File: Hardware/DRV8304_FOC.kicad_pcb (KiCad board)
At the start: 4 copper layers, 51.5 x 42.8 mm, 64 parts, among them J1 Conn_01x02, J2 Conn_01x03, J3 Conn_01x03, J4 Conn_02x07_Counter_Clockwise, Q1 SIRA18ADP, Q2 SIRA18ADP, Q3 SIRA18ADP, Q4 SIRA18ADP, Q5 SIRA18ADP, Q6 SIRA18ADP, SW2 SW_Push, U1 TPS565208, U2 TPS259850RQPR, U3 DRV8304HRHAR, U4 STM32F412CEUx, U5 AS5055A, Y1 Crystal_GND23

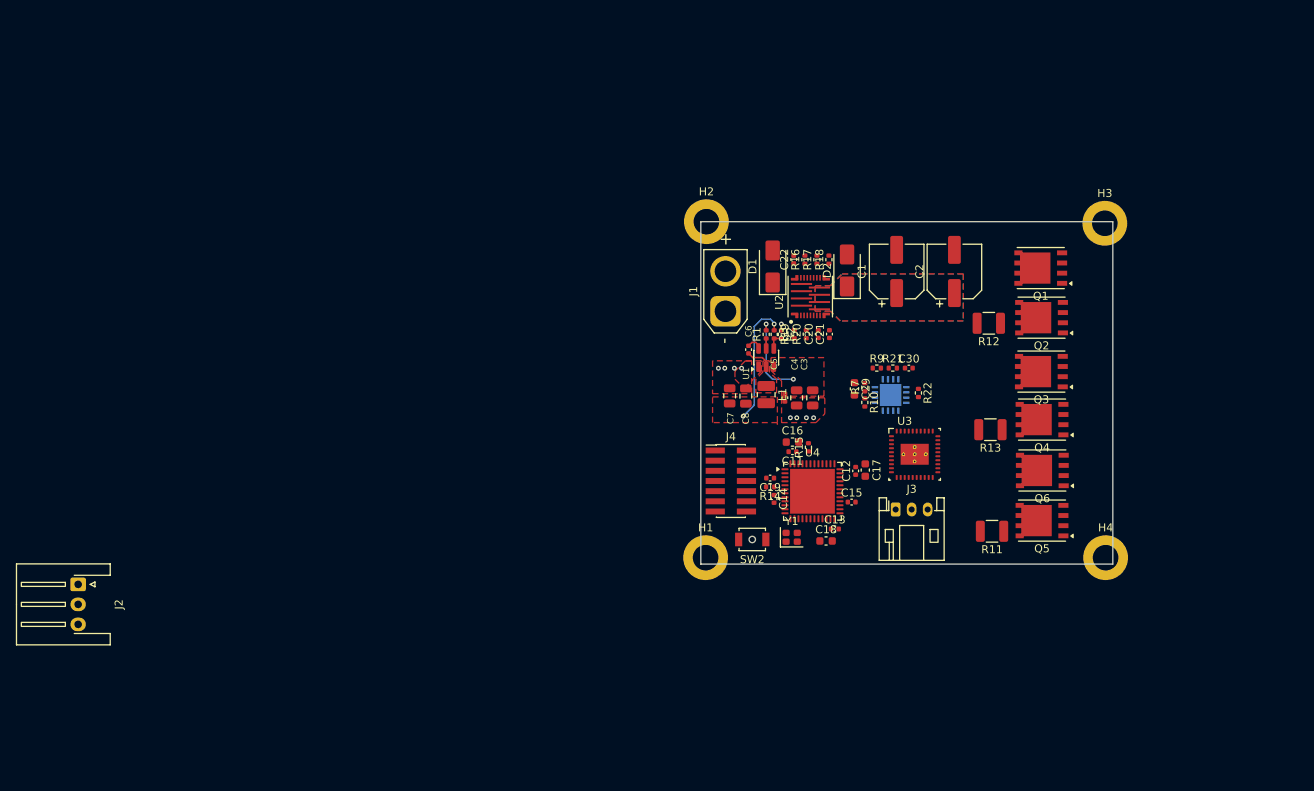
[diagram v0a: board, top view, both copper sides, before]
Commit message: Added Board outline DXF and test points
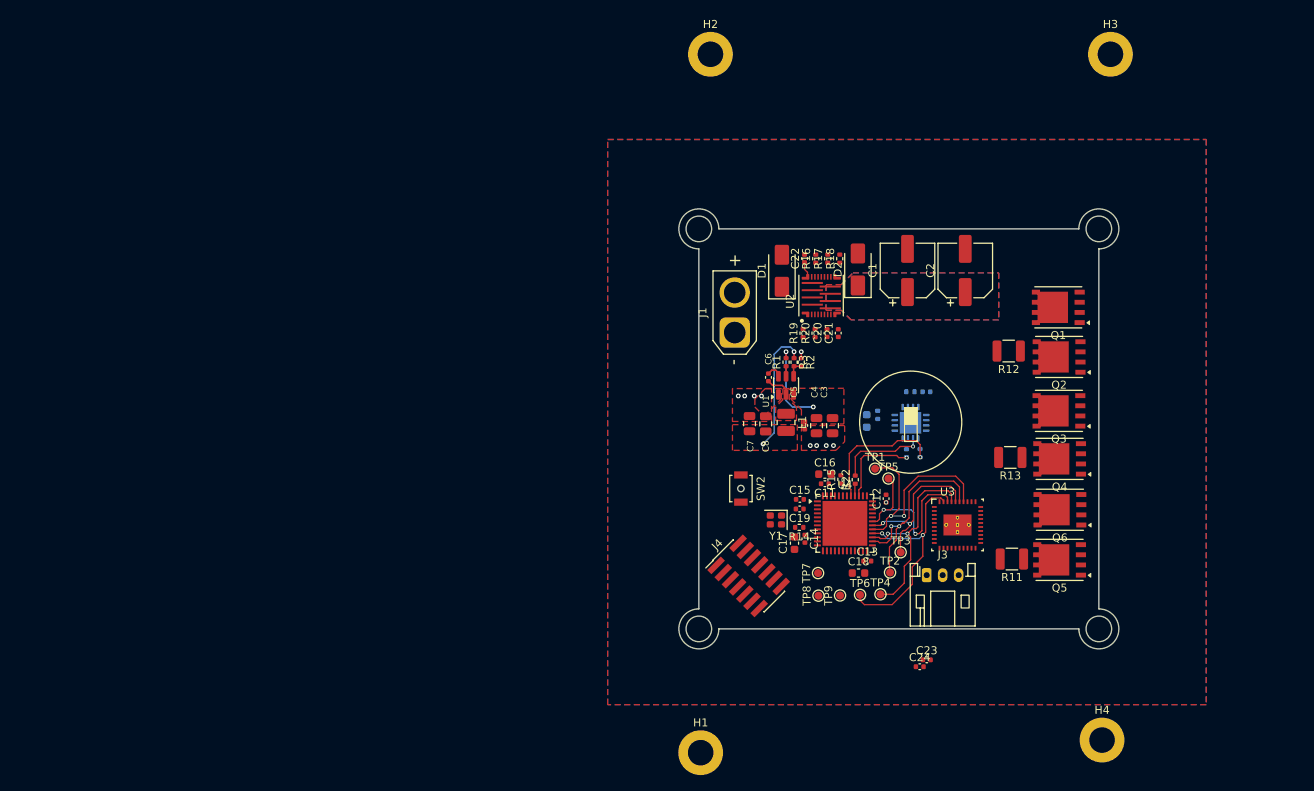
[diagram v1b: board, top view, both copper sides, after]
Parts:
- removed J2: Conn_01x03, Connector_JST:JST_XH_S3B-XH-A-1_1x03_P2.50mm_Horizontal
- added C23: 0.1uF, Capacitor_SMD:C_0402_1005Metric, F.Cu at (164.1, 126.4)
- added C24: 0.1uF, Capacitor_SMD:C_0402_1005Metric, F.Cu at (163.2, 127.3)
- added TP1: TestPoint, TestPoint:TestPoint_Pad_D1.0mm, F.Cu at (157.6, 102.5)
- added TP2: TestPoint, TestPoint:TestPoint_Pad_D1.0mm, F.Cu at (159.5, 115.5)
- added TP3: TestPoint, TestPoint:TestPoint_Pad_D1.0mm, F.Cu at (160.8, 113.0)
- added TP4: TestPoint, TestPoint:TestPoint_Pad_D1.0mm, F.Cu at (158.3, 118.2)
- added TP5: TestPoint, TestPoint:TestPoint_Pad_D1.0mm, F.Cu at (159.3, 103.8)
- added TP6: TestPoint, TestPoint:TestPoint_Pad_D1.0mm, F.Cu at (155.7, 118.3)
- added TP7: TestPoint, TestPoint:TestPoint_Pad_D1.0mm, F.Cu at (150.5, 115.6)
- added TP8: TestPoint, TestPoint:TestPoint_Pad_D1.0mm, F.Cu at (150.5, 118.4)
- added TP9: TestPoint, TestPoint:TestPoint_Pad_D1.0mm, F.Cu at (153.2, 118.4)
- C29, C30, R10, R21, R7, R9: moved to B.Cu
- moved H1 24.4 mm to (135.8, 138.0)
- moved H4 22.8 mm to (186.0, 136.5)
- moved H3 21.1 mm to (187.0, 50.7)
- moved H2 20.9 mm to (137.0, 50.7)
- moved R22 13.4 mm to (155.1, 103.9), turned to 90 degrees
- moved C17 12.7 mm to (147.5, 111.8), turned to 90 degrees
- moved J4 12.1 mm to (141.8, 115.9), turned to 45 degrees
- moved R9 11.9 mm to (163.2, 100.6), turned to 90 degrees
- moved U3 10.3 mm to (167.9, 109.6)
- moved J3 9.08 mm to (164.1, 115.8)
- moved R10 8.21 mm to (161.5, 100.6), turned to 90 degrees
- moved SW2 6.52 mm to (140.8, 105.0), turned to -90 degrees
- moved C15 6.48 mm to (148.2, 106.4)
- moved C14 6.30 mm to (148.8, 111.3)
- moved R14 6.23 mm to (148.1, 109.9)
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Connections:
- J3 pad 1: unconnected-(J3-Pin_1-Pad1) -> GND
- J3 pad 2: unconnected-(J3-Pin_2-Pad2) -> UART_RX
- J3 pad 3: unconnected-(J3-Pin_3-Pad3) -> UART_TX
- Q1 pad 1: Vin -> Net-(Q1-D)
- Q1 pad 2: unconnected-(Q1-G-Pad2) -> Net-(Q1-D)
- Q1 pad 3: Net-(Q1-S) -> Net-(Q1-D)
- Q1 pad 4: (no net) -> GHA
- Q1 pad 5: (no net) -> Vin
- Q2 pad 1: Net-(Q1-S) -> Net-(Q2-D)
- Q2 pad 2: unconnected-(Q2-G-Pad2) -> Net-(Q2-D)
- Q2 pad 3: Net-(Q2-S) -> Net-(Q2-D)
- Q2 pad 4: (no net) -> GLA
- Q2 pad 5: (no net) -> Net-(Q1-D)
- Q3 pad 1: Vin -> Net-(Q3-D)
- Q3 pad 2: unconnected-(Q3-G-Pad2) -> Net-(Q3-D)
- Q3 pad 3: Net-(Q3-S) -> Net-(Q3-D)
- Q3 pad 4: (no net) -> unconnected-(Q3-G-Pad4)
- Q3 pad 5: (no net) -> Vin
- Q4 pad 1: Net-(Q3-S) -> Net-(Q4-D)
- Q4 pad 2: unconnected-(Q4-G-Pad2) -> Net-(Q4-D)
- Q4 pad 3: Net-(Q4-S) -> Net-(Q4-D)
- Q4 pad 4: (no net) -> unconnected-(Q4-G-Pad4)
- Q4 pad 5: (no net) -> Net-(Q3-D)
- Q5 pad 1: Vin -> Net-(Q5-D)
- Q5 pad 2: unconnected-(Q5-G-Pad2) -> Net-(Q5-D)
- Q5 pad 3: Net-(Q5-S) -> Net-(Q5-D)
- Q5 pad 4: (no net) -> unconnected-(Q5-G-Pad4)
- Q5 pad 5: (no net) -> Vin
- Q6 pad 1: Net-(Q5-S) -> Net-(Q6-D)
- Q6 pad 2: unconnected-(Q6-G-Pad2) -> Net-(Q6-D)
- Q6 pad 3: Net-(Q6-S) -> Net-(Q6-D)
- Q6 pad 4: (no net) -> unconnected-(Q6-G-Pad4)
- Q6 pad 5: (no net) -> Net-(Q5-D)
- R10 pad 1: SCK -> SPI_SCK
- R11 pad 1: Net-(Q2-S) -> Net-(Q2-D)
- R12 pad 1: Net-(Q4-S) -> Net-(Q4-D)
- R13 pad 1: Net-(Q6-S) -> Net-(Q6-D)
- R22 pad 1: Net-(U5-MISO) -> Net-(U4-PB4)
- R22 pad 2: MISO -> SPI_MISO
- R9 pad 1: MOSI -> SPI_MOSI
- U3 pad 21: unconnected-(U3-SOC-Pad21) -> ISENSE_C
- U3 pad 22: unconnected-(U3-SOB-Pad22) -> ISENSE_B
- U3 pad 23: unconnected-(U3-SOA-Pad23) -> ISENSE_A
- U3 pad 34: unconnected-(U3-INHA-Pad34) -> INHA
- U3 pad 35: unconnected-(U3-INLA-Pad35) -> INLA
- U3 pad 36: unconnected-(U3-INHB-Pad36) -> INHB
- U3 pad 37: unconnected-(U3-INLB-Pad37) -> INLB
- U3 pad 38: unconnected-(U3-INHC-Pad38) -> INHC
- U3 pad 39: unconnected-(U3-INLC-Pad39) -> INLC
- U4 pad 13: unconnected-(U4-PA3-Pad13) -> ISENSE_C
- U4 pad 14: unconnected-(U4-PA4-Pad14) -> ISENSE_B
- U4 pad 15: unconnected-(U4-PA5-Pad15) -> ISENSE_A
- U4 pad 20: unconnected-(U4-PB2-Pad20) -> SPI_~{SS}
- U4 pad 26: unconnected-(U4-PB13-Pad26) -> INLA
- U4 pad 27: unconnected-(U4-PB14-Pad27) -> INLB
- U4 pad 28: unconnected-(U4-PB15-Pad28) -> INLC
- U4 pad 29: unconnected-(U4-PA8-Pad29) -> INHA
- U4 pad 30: unconnected-(U4-PA9-Pad30) -> INHB
- U4 pad 31: unconnected-(U4-PA10-Pad31) -> INHC
- U4 pad 39: unconnected-(U4-PB3-Pad39) -> SPI_SCK
- U4 pad 40: unconnected-(U4-PB4-Pad40) -> Net-(U4-PB4)
- U4 pad 41: unconnected-(U4-PB5-Pad41) -> SPI_MOSI
- U4 pad 43: unconnected-(U4-PB7-Pad43) -> UART_RX
- U4 pad 45: unconnected-(U4-PB8-Pad45) -> UART_TX
- U4 pad 5: unconnected-(U4-PH0-Pad5) -> Net-(U4-PH0)
- U4 pad 6: unconnected-(U4-PH1-Pad6) -> Net-(U4-PH1)
- U5 pad 2: Net-(U5-MISO) -> SPI_MISO
- U5 pad 4: ~{SS} -> SPI_~{SS}
- Y1 pad 1: unconnected-(Y1-Pad1) -> Net-(U4-PH0)
- Y1 pad 4: unconnected-(Y1-Pad4) -> Net-(U4-PH1)
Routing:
- net INLC: track 0.00 -> 28.8 mm, vias 0 -> 2
- net INHA: track 0.00 -> 28.6 mm, vias 0 -> 2
- net INLB: track 0.00 -> 26.1 mm, vias 0 -> 2
- net INLA: track 0.00 -> 25.5 mm, vias 0 -> 2
- net INHC: track 0.00 -> 23.1 mm, vias 0 -> 2
- net INHB: track 0.00 -> 20.7 mm, vias 0 -> 2
- net SPI_MOSI: track 0.00 -> 16.7 mm, vias 0 -> 1
- net SPI_MISO: track 0.00 -> 11.1 mm, vias 0 -> 1
- net SPI_SCK: track 0.00 -> 10.7 mm, vias 0 -> 1
- net Net-(U2-VDD): track 0.00 -> 2.10 mm
- net Net-(U4-PB4): track 0.00 -> 1.53 mm
- net GND: vias 9 -> 10
- added copper zone on B.Cu, net GND
- added copper zone on In1.Cu, net GND
- added copper zone on In2.Cu, net GND
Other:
- board size 51.5 x 42.8 mm -> 55 x 55 mm

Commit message: Routing update
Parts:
- TP1, TP2, TP3, TP4, TP5, TP6, TP7, TP8, TP9: footprint TestPoint:TestPoint_Pad_D1.0mm -> MyLib:TestPoint_1mm
- moved Q5 31.5 mm to (180.7, 82.4)
- moved Q1 25.8 mm to (180.5, 108.2)
- moved Q2 25.2 mm to (180.5, 113.8), turned to 0 degrees
- moved TP8 22.1 mm to (167.7, 104.6)
- moved TP7 21.6 mm to (169.1, 104.6)
- moved Q6 19.7 mm to (180.6, 88.0), turned to 0 degrees
- moved TP9 19.0 mm to (166.3, 104.6)
- moved R13 13.6 mm to (173.7, 87.6)
- moved R12 12.5 mm to (173.7, 100.4)
- moved J3 12.5 mm to (169.8, 127.0)
- moved TP5 7.07 mm to (160.3, 110.8)
- moved TP1 6.42 mm to (160.3, 108.4)
- moved TP6 6.04 mm to (160.3, 114.4)
- moved TP4 5.46 mm to (160.3, 113.2)
- moved J1 3.66 mm to (139.9, 81.9)
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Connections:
- Q1 pad 1: Net-(Q1-D) -> SHA
- Q1 pad 2: Net-(Q1-D) -> SHA
- Q1 pad 3: Net-(Q1-D) -> SHA
- Q2 pad 5: Net-(Q1-D) -> SHA
- Q3 pad 1: Net-(Q3-D) -> SHB
- Q3 pad 2: Net-(Q3-D) -> SHB
- Q3 pad 3: Net-(Q3-D) -> SHB
- Q3 pad 4: unconnected-(Q3-G-Pad4) -> GHB
- Q4 pad 4: unconnected-(Q4-G-Pad4) -> GLB
- Q4 pad 5: Net-(Q3-D) -> SHB
- Q5 pad 1: Net-(Q5-D) -> SHC
- Q5 pad 2: Net-(Q5-D) -> SHC
- Q5 pad 3: Net-(Q5-D) -> SHC
- Q5 pad 4: unconnected-(Q5-G-Pad4) -> GHC
- Q6 pad 4: unconnected-(Q6-G-Pad4) -> GLC
- Q6 pad 5: Net-(Q5-D) -> SHC
- U4 pad 26: INLA -> INLC
- U4 pad 28: INLC -> INLA
- U4 pad 29: INHA -> INHC
- U4 pad 31: INHC -> INHA
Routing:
- net ISENSE_C: track 0.00 -> 37.6 mm, vias 0 -> 2
- net ISENSE_B: track 0.00 -> 34.3 mm, vias 0 -> 2
- net ISENSE_A: track 0.00 -> 33.1 mm, vias 0 -> 2
- net INHA: track 28.6 -> 6.40 mm, vias 2 -> 0
- net INLC: track 28.8 -> 9.94 mm, vias 2 -> 0
- net INHC: track 23.1 -> 6.16 mm, vias 2 -> 0
- net INLA: track 25.5 -> 9.72 mm
- net INLB: track 26.1 -> 10.6 mm
- net INHB: track 20.7 -> 6.03 mm, vias 2 -> 0
- net 3V3: track 0.00 -> 6.80 mm
- net GHA: track 0.00 -> 6.55 mm, vias 0 -> 1
- net SHA: track 0.00 -> 5.43 mm, vias 0 -> 1
- net Net-(U4-PH1): track 0.00 -> 4.63 mm
- net Net-(U4-PH0): track 0.00 -> 4.59 mm
- net GLA: track 0.00 -> 4.31 mm, vias 0 -> 1
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
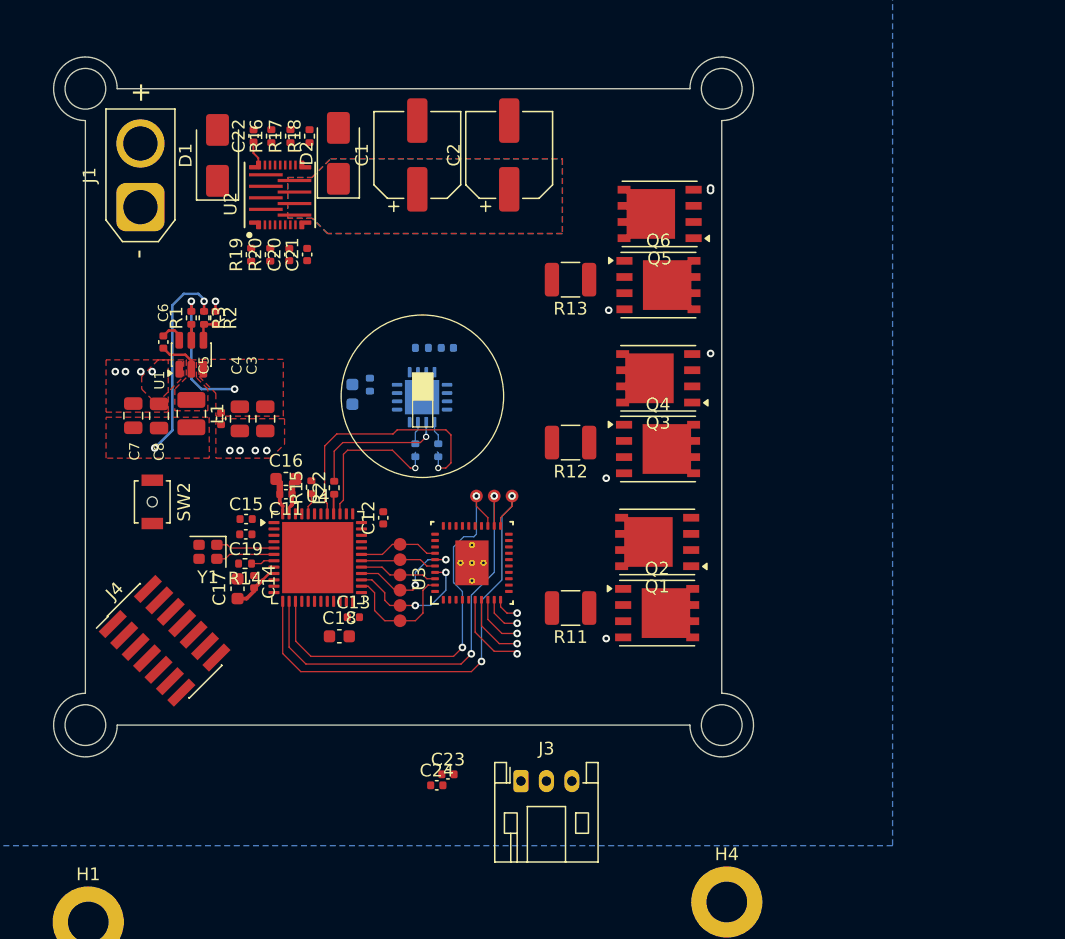
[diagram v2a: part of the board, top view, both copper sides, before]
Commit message: Remove EFUSE
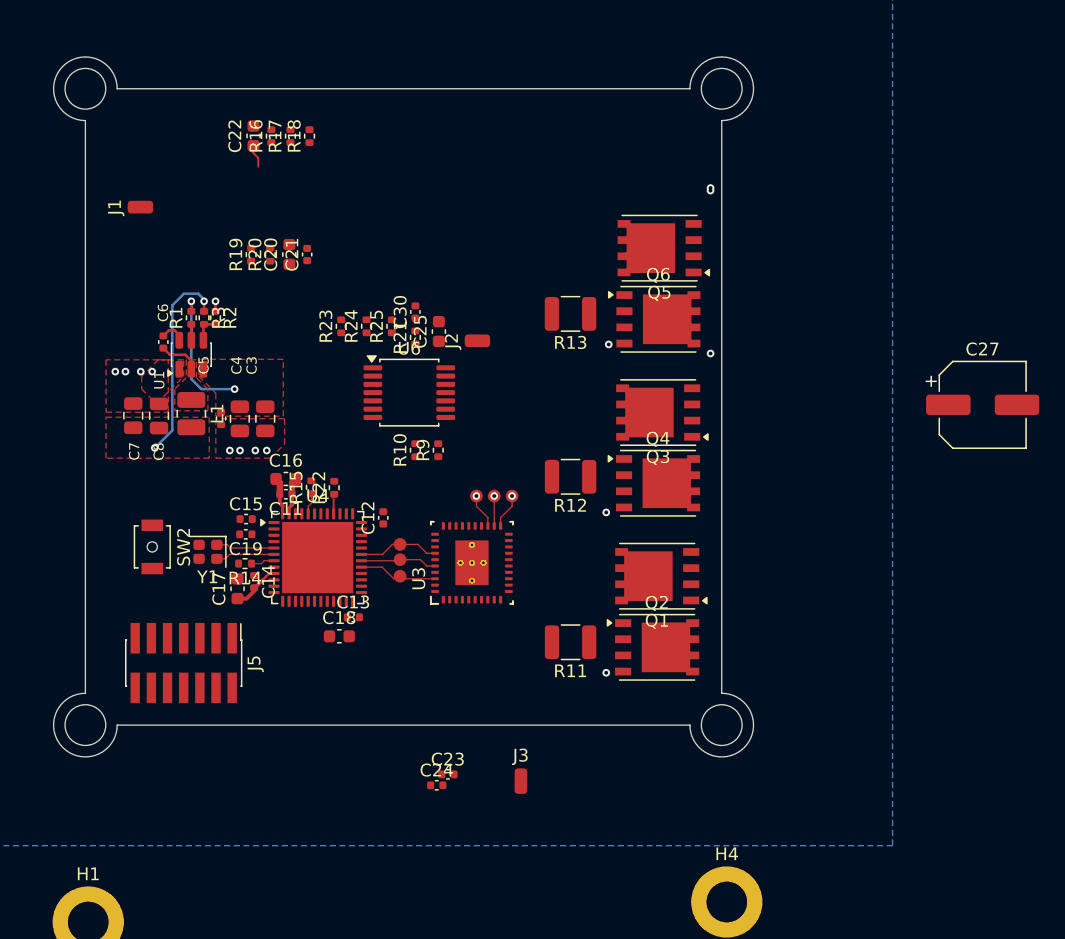
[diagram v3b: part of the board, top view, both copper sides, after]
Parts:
- removed C1, C2: C_Polarized, Capacitor_SMD:CP_Elec_6.3x7.7
- removed C29: 4.7uF, Capacitor_SMD:C_0603_1608Metric
- removed D1: 20V, Diode_SMD:D_SMA
- removed D2: D_Schottky, Diode_SMD:D_SMA
- removed J4: Conn_02x07_Counter_Clockwise, Connector_PinHeader_1.27mm:PinHeader_2x07_P1.27mm_Vertical_SMD
- removed R7: 15R, Resistor_SMD:R_0402_1005Metric
- removed TP2, TP4, TP6: TestPoint, MyLib:TestPoint_1mm
- removed U2: TPS259850RQPR, 1_MyLib:RQP0026A-MFG
- removed U5: AS5055A, Package_DFN_QFN:QFN-16-1EP_4x4mm_P0.65mm_EP2.7x2.7mm
- added C25: 1uF, Capacitor_SMD:C_0603_1608Metric, F.Cu at (163.4, 91.6)
- added C27: 100uF, Capacitor_SMD:CP_Elec_6.3x7.7, F.Cu at (206.1, 97.4)
- added J2: Conn_01x01_Pin, Connector_Wire:SolderWirePad_1x01_SMD_1x2mm, F.Cu at (166.4, 92.4)
- added J5: Conn_02x07_Odd_Even, Connector_PinHeader_1.27mm:PinHeader_2x07_P1.27mm_Vertical_SMD, F.Cu at (143.3, 117.7)
- added R23: 0R, Resistor_SMD:R_0402_1005Metric, F.Cu at (155.7, 91.2)
- added R24: 0R, Resistor_SMD:R_0402_1005Metric, F.Cu at (157.7, 91.2)
- added R25: 10k, Resistor_SMD:R_0402_1005Metric, F.Cu at (159.7, 91.2)
- added U6: AS5047P, Package_SO:TSSOP-14_4.4x5mm_P0.65mm, F.Cu at (161.0, 96.4)
- C20: value 43nF -> 1uF; footprint Capacitor_SMD:C_0402_1005Metric -> Capacitor_SMD:C_0603_1608Metric
- C21: value 3.3nF -> 22nF
- C22: value 0.1uF -> 1uF; footprint Capacitor_SMD:C_0402_1005Metric -> Capacitor_SMD:C_0603_1608Metric
- C30, R10, R9: moved to F.Cu
- J1: value Conn_01x02 -> Conn_01x01_Pin; footprint Connector_AMASS:AMASS_XT30U-M_1x02_P5.0mm_Vertical -> Connector_Wire:SolderWirePad_1x01_SMD_1x2mm
- J3: value Conn_01x03 -> Conn_01x01_Pin; footprint Connector_JST:JST_PH_S3B-PH-K_1x03_P2.00mm_Horizontal -> Connector_Wire:SolderWirePad_1x01_SMD_1x2mm
- R16: value 40k -> 47k
- R17, R18: value 1.5k -> 0R
- R19, R20: value 100k -> 0R
- R21: value 10k -> 0R; moved to F.Cu
- moved C30 3.78 mm to (161.5, 90.1), turned to 90 degrees
- moved SW2 3.54 mm to (140.8, 108.6)
- moved Q5 2.69 mm to (180.7, 85.1)
- moved Q1 2.69 mm to (180.5, 110.9)
- moved Q2 2.69 mm to (180.5, 116.5)
- moved Q3 2.69 mm to (180.6, 98.0)
- moved Q4 2.69 mm to (180.6, 103.6)
- moved Q6 2.69 mm to (180.6, 90.7)
- moved R11 2.69 mm to (173.7, 116.1)
- moved R12 2.69 mm to (173.7, 103.1)
- moved R13 2.69 mm to (173.7, 90.3)
- moved R21 0.97 mm to (161.5, 92.1), turned to 90 degrees
- moved TP5 0.10 mm to (160.3, 110.9)
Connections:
- net Net-(U4-NRST) renamed /~{RST}
- C20 pad 1: Net-(U2-ITIMER) -> GND
- C20 pad 2: GND -> Net-(U3-DVDD)
- C21 pad 1: Net-(U2-DVDT) -> Net-(U3-CPH)
- C21 pad 2: GND -> Net-(U3-CPL)
- C22 pad 1: Net-(U2-VDD) -> Vin
- C22 pad 2: GND -> Net-(U3-VCP)
- J1 pad 1: Vin -> UART_TX
- R16 pad 2: Net-(U2-IREF) -> Net-(U3-MODE/SDO)
- R17 pad 1: GND -> Net-(U3-MODE/SDO)
- R17 pad 2: Net-(U2-IMON) -> 3V3
- R18 pad 1: Net-(U2-ILIM) -> Net-(U3-IDRIVE/SDI)
- R18 pad 2: GND -> 3V3
- R19 pad 1: Net-(U2-SWEN) -> GND
- R19 pad 2: Net-(U2-ILIM) -> Net-(U3-IDRIVE/SDI)
- R20 pad 1: Vin -> Net-(U3-GAIN/~{CS})
- R20 pad 2: Net-(U2-VDD) -> 3V3
- R21 pad 1: 3V3 -> GND
- R21 pad 2: ~{INT} -> Net-(U3-GAIN/~{CS})
- U3 pad 1: unconnected-(U3-CPL-Pad1) -> Net-(U3-CPL)
- U3 pad 2: unconnected-(U3-CPH-Pad2) -> Net-(U3-CPH)
- U3 pad 24: unconnected-(U3-VREF-Pad24) -> 3V3
- U3 pad 26: unconnected-(U3-SDO-Pad26) -> Net-(U3-MODE/SDO)
- U3 pad 27: unconnected-(U3-SDI-Pad27) -> Net-(U3-IDRIVE/SDI)
- U3 pad 28: unconnected-(U3-SCLK-Pad28) -> Net-(U3-VDS/SCLK)
- U3 pad 29: unconnected-(U3-SCS_N-Pad29) -> Net-(U3-GAIN/~{CS})
- U3 pad 3: unconnected-(U3-VCP-Pad3) -> Net-(U3-VCP)
- U3 pad 30: unconnected-(U3-ENABLE-Pad30) -> 3V3
- U3 pad 31: unconnected-(U3-CAL-Pad31) -> Net-(U3-CAL)
- U3 pad 32: unconnected-(U3-AGND-Pad32) -> GND
- U3 pad 33: unconnected-(U3-DVDD-Pad33) -> Net-(U3-DVDD)
- U3 pad 35: INLA -> 3V3
- U3 pad 37: INLB -> 3V3
- U3 pad 39: INLC -> 3V3
- U3 pad 4: unconnected-(U3-VM-Pad4) -> Vin
- U3 pad 40: unconnected-(U3-PGND-Pad40) -> GND
- U3 pad 41: unconnected-(U3-PAD-Pad41) -> GND
- U3 pad 5: unconnected-(U3-VDRAIN-Pad5) -> Vin
- U4 pad 26: INLC -> unconnected-(U4-PB13-Pad26)
- U4 pad 27: INLB -> unconnected-(U4-PB14-Pad27)
- U4 pad 28: INLA -> unconnected-(U4-PB15-Pad28)
- U4 pad 32: unconnected-(U4-PA11-Pad32) -> /VCP_TX
- U4 pad 33: unconnected-(U4-PA12-Pad33) -> /VCP_RX
- U4 pad 34: unconnected-(U4-PA13-Pad34) -> /SWDIO
- U4 pad 37: unconnected-(U4-PA14-Pad37) -> /SWCLK
- U4 pad 42: unconnected-(U4-PB6-Pad42) -> UART_TX
- U4 pad 45: UART_TX -> unconnected-(U4-PB8-Pad45)
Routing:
- net ISENSE_C: track 37.6 -> 2.92 mm, vias 2 -> 1
- net ISENSE_B: track 34.3 -> 2.35 mm, vias 2 -> 1
- net ISENSE_A: track 33.1 -> 2.72 mm, vias 2 -> 1
- net SPI_MOSI: track 20.7 -> 0.00 mm, vias 1 -> 0
- net SPI_SCK: track 12.4 -> 0.00 mm, vias 1 -> 0
- net SPI_MISO: track 11.2 -> 0.00 mm, vias 1 -> 0
- net INLB: track 10.6 -> 0.00 mm, vias 2 -> 0
- net INLC: track 9.94 -> 0.00 mm
- net INLA: track 9.72 -> 0.00 mm, vias 2 -> 0
- net GHA: track 6.55 -> 0.00 mm, vias 1 -> 0
- net SHA: track 5.43 -> 0.00 mm, vias 1 -> 0
- net GLA: track 4.31 -> 0.00 mm, vias 1 -> 0
- net SPA: track 3.18 -> 0.00 mm, vias 1 -> 0
- net Vin: track 0.00 -> 2.10 mm
- net Net-(U2-VDD): track 2.10 -> 0.00 mm
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- removed copper zone on B.Cu, net Vm
- removed copper zone on F.Cu, net Vm
- removed copper zone on In1.Cu, net Vm
- removed copper zone on In2.Cu, net Vm
